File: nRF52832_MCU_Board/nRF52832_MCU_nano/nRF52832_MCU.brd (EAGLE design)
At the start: 55.7 x 22.9 mm, 56 parts, among them J1 TSW-116-02-S-S, J2 TSW-116-02-S-S, J3 MM8130-2600, J4 FPC_05P-RA-SMD, J5 DEBUG_CONNECTOR, U1 NRF52832, X1 32MHz, X2 32.768kHz, X3 TSW-102-02-S-S-RA, X4 TSW-102-02-S-S-RA, X5 TSW-103-02-S-S, X6 TSW-103-02-S-S

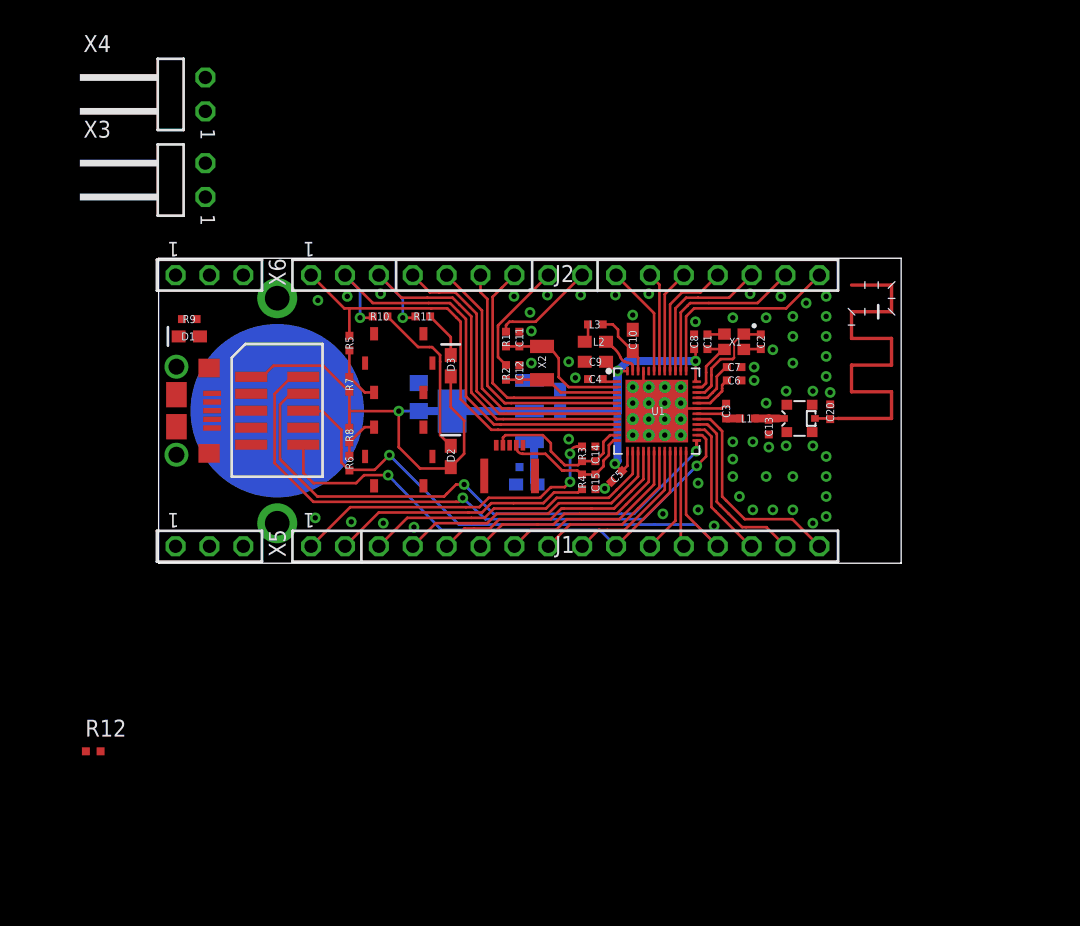
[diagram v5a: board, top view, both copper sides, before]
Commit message: Connected all signals in layout
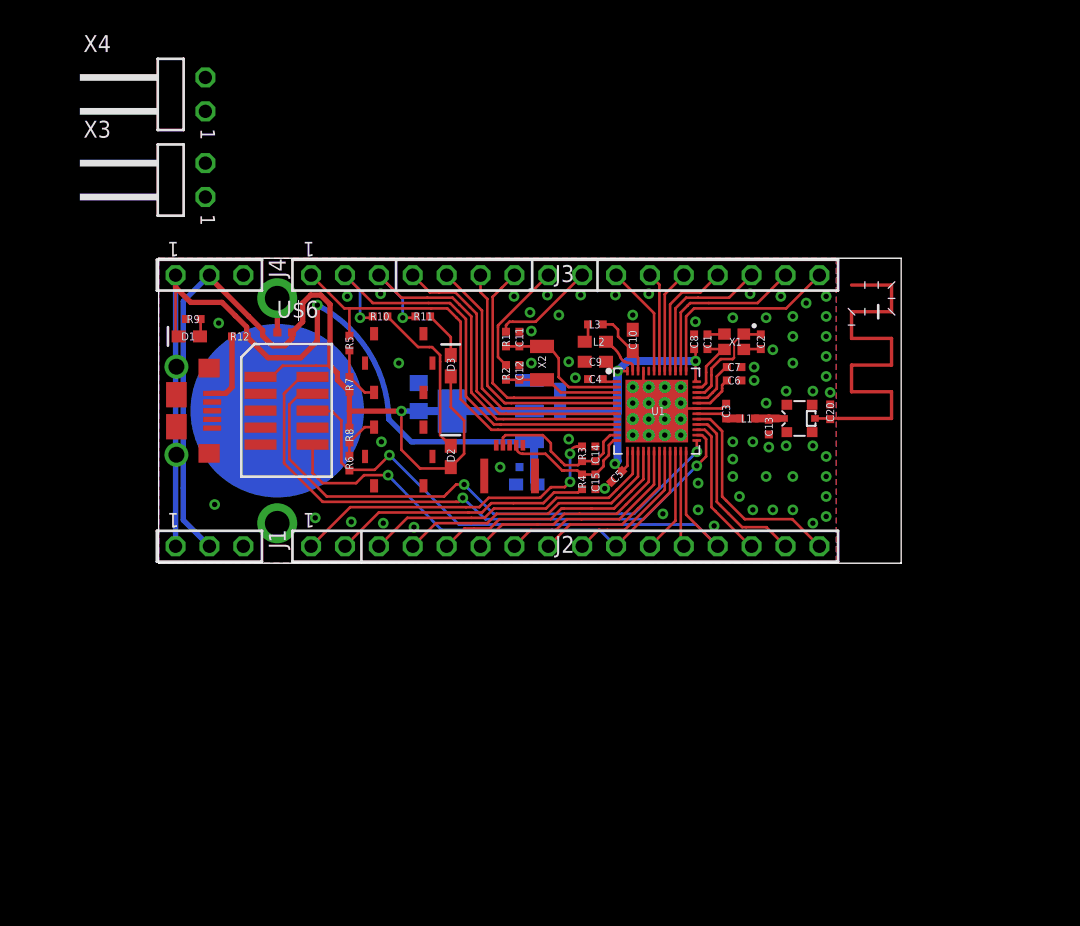
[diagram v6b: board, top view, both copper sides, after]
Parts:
- removed U$1: MICROUSB, Nordic_misc:USB-MICRO-B-RA-SMD-PIP
- removed X5, X6: TSW-103-02-S-S, con-samtec:TSW-103-02-S-S
- added J6: DEBUG_CONNECTOR, Nordic_misc:HDRV127P5X2-10_N
- added J7: FPC_05P-RA-SMD, Nordic_misc:FPC_05P-RA-SMD
- added J8: MM8130-2600, Nordic_misc:MM8130-2600
- added U$6: 0R, Nordic_misc:RESC0402_N
- C13: value (none) -> N.C.
- C20: value (none) -> TBD
- J1: value TSW-116-02-S-S -> TSW-103-02-S-S; device con-samtec:TSW-116-02-S-S -> con-samtec:TSW-103-02-S-S
- J3: value MM8130-2600 -> TSW-116-02-S-S; device Nordic_misc:MM8130-2600 -> con-samtec:TSW-116-02-S-S
- J4: value FPC_05P-RA-SMD -> TSW-103-02-S-S; device Nordic_misc:FPC_05P-RA-SMD -> con-samtec:TSW-103-02-S-S
- J5: value DEBUG_CONNECTOR -> MICROUSB; device Nordic_misc:HDRV127P5X2-10_N -> Nordic_misc:USB-MICRO-B-RA-SMD-PIP
- moved R12 33.0 mm to (6.05, 17.0)
- moved J4 26.7 mm to (3.81, 21.6), turned to 180 degrees
- moved J1 26.7 mm to (3.81, 1.27)
- moved J3 20.6 mm to (30.5, 21.6), turned to 180 degrees
- moved J2 20.3 mm to (30.5, 1.27)
- moved J5 4.88 mm to (4.01, 11.4), turned to 0 degrees
- moved R9 0.30 mm to (2.60, 18.3)
- renumbered U$2 to U2, U$3 to BATT1
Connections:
- new net VDD_P3V3_BATT: BATT1.2, BATT1.3, U$6.1
- net GND: now also BATT1.1, J1.3, J4.3, J6.3, J6.5, J6.9, J8.1, J8.2, J8.3, J8.4; no longer J3.1, J3.2, J3.3, J3.4, J5.3, J5.9, U$1.5, X5.3, X6.3
- net N$1: now also J8.OUT; no longer J3.OUT
- net N$5: now also J8.IN; no longer J3.IN
- net NFC1: now also J7.2; no longer J4.2
- net NFC2: now also J7.4; no longer J4.4
- net P0.00: now also J3.9; no longer J2.9
- net P0.01: now also J3.8; no longer J2.8
- net P0.02: now also J3.7; no longer J2.7
- net P0.03: now also J3.6; no longer J2.6
- net P0.04: now also J3.5; no longer J2.5
- net P0.05: now also J3.4; no longer J2.4
- net P0.06: now also J3.3; no longer J2.3
- net P0.07: now also J3.2; no longer J2.2
- net P0.08: now also J3.1; no longer J2.1
- net P0.09: now also J2.1; no longer J1.1
- net P0.10: now also J2.2; no longer J1.2
- net P0.11: now also J2.3; no longer J1.3
- net P0.12: now also J2.4; no longer J1.4
- net P0.13: now also J2.5; no longer J1.5
- net P0.14: now also J2.6; no longer J1.6
- net P0.15: now also J2.7; no longer J1.7
- net P0.16: now also J2.8; no longer J1.8
- net P0.17: now also J2.9; no longer J1.9
- net P0.18/SWO: now also J2.10, J6.10; no longer J1.10, J5.10
- net P0.19: now also J2.11; no longer J1.11
- net P0.20: now also J2.12; no longer J1.12
- net P0.21/RESET: now also J2.13, J6.6; no longer J1.13, J5.6
- net P0.22: now also J2.14; no longer J1.14
- net P0.23: now also J2.15; no longer J1.15
- net P0.24: now also J2.16; no longer J1.16
- net P0.25: now also J3.16; no longer J2.16
- net P0.26: now also J3.15; no longer J2.15
- net P0.27: now also J3.14; no longer J2.14
- net P0.28: now also J3.13; no longer J2.13
- net P0.29: now also J3.12; no longer J2.12
- net P0.30: now also J3.11; no longer J2.11
- net P0.31: now also J3.10; no longer J2.10
- net SWDCLK: now also J6.4; no longer J5.4
- net SWDIO: now also J6.2; no longer J5.2
- net VCC_P5V0_USB: now also J5.1; no longer U$1.1
- net VDD_P3V3: now also J1.2, J4.2, J6.1, U$6.2; no longer J5.1, X5.2, X6.2
- net VDD_P5V0: now also J1.1, J4.1; no longer X5.1, X6.1
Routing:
- net VDD_P5V0: track 3.45 -> 67.1 mm, vias 0 -> 1
- net VDD_P3V3: track 70.9 -> 111.4 mm
- net VCC_P5V0_USB: track 0.00 -> 5.48 mm
- net VDD_P3V3_BATT: track 0.00 -> 2.57 mm
- net SWDCLK: track 43.4 -> 41.9 mm
- net VDD_LED: track 0.00 -> 1.30 mm
- net SWDIO: track 46.2 -> 45.5 mm
- net P0.18/SWO: track 37.2 -> 36.5 mm
- net GND: vias 63 -> 67
- added copper zone on layer 1, net GND
- added copper zone on layer 16, net GND

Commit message: Looked at arduino layout
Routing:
- net N$7: track 4.33 -> 6.69 mm
- net GND: vias 67 -> 68
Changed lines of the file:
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@@
 <grid distance="0.1" unitdist="mm" unit="mm" style="lines" multiple="2" display="yes" altdistance="0.05" altunitdist="mm" altunit="mm"/>
 <layers>
-<layer number="1" name="Top" color="4" fill="1" visible="no" active="yes"/>
+<layer number="1" name="Top" color="4" fill="1" visible="yes" active="yes"/>
 <layer number="16" name="Bottom" color="1" fill="1" visible="yes" active="yes"/>
 <layer number="17" name="Pads" color="2" fill="1" visible="yes" active="yes"/>
@@
 <via x="4.2" y="4.4" extent="1-16" drill="0.4"/>
 <via x="4.5" y="18" extent="1-16" drill="0.4"/>
-<wire x1="19.85" y1="17.2" x2="20.525" y2="15" width="0" layer="19" extent="1-1"/>
+<via x="20.9" y="16.9" extent="1-16" drill="0.4"/>
 </signal>
 <signal name="DEC1">
@@
 <wire x1="14.3" y1="13.95" x2="15.45" y2="12.8" width="0.2" layer="1"/>
 <wire x1="15.45" y1="12.8" x2="16.15" y2="12.8" width="0.2" layer="1"/>
-<wire x1="14.3" y1="15.95" x2="16.15" y2="17.2" width="0" layer="19" extent="1-1"/>
+<wire x1="14.3" y1="15.95" x2="15.55" y2="17.2" width="0.2" layer="1"/>
+<wire x1="15.55" y1="17.2" x2="16.15" y2="17.2" width="0.2" layer="1"/>
 </signal>
 <signal name="VDD_P3V3">

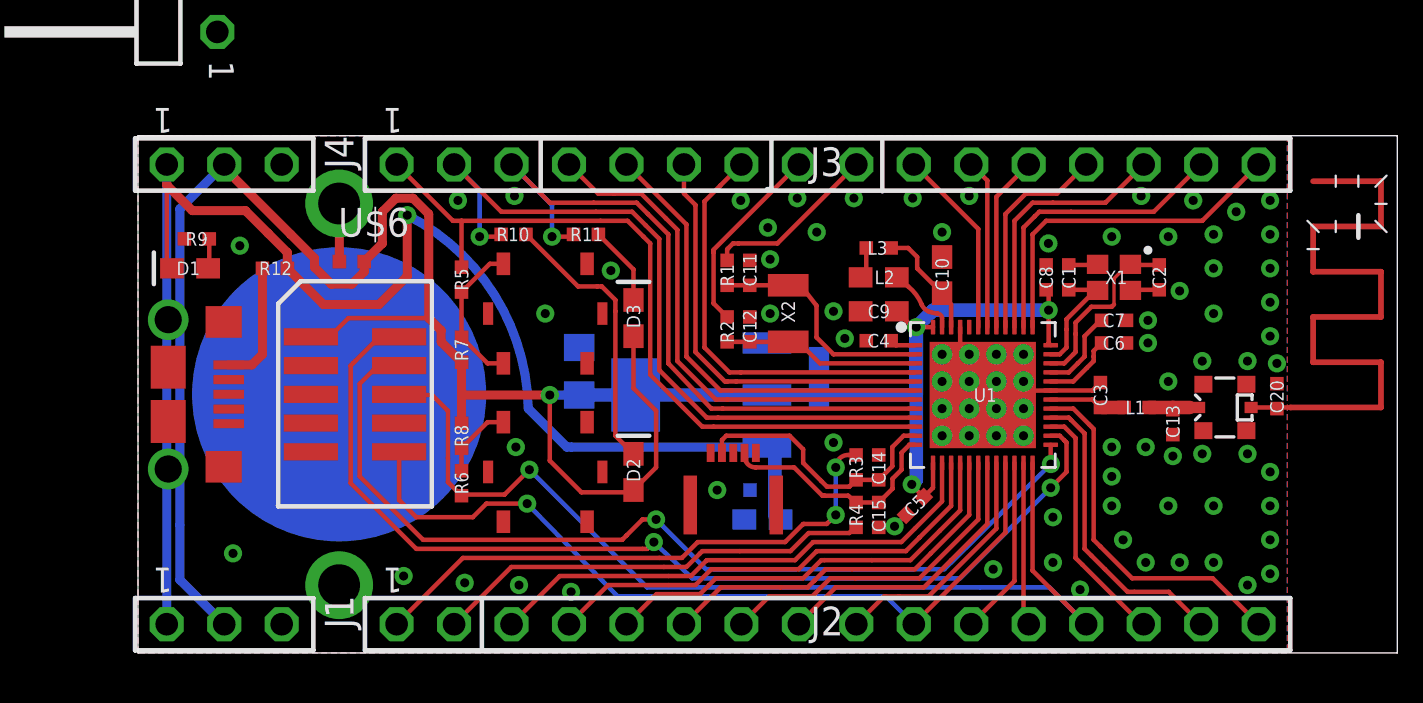
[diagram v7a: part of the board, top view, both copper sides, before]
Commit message: Cleanup in layout
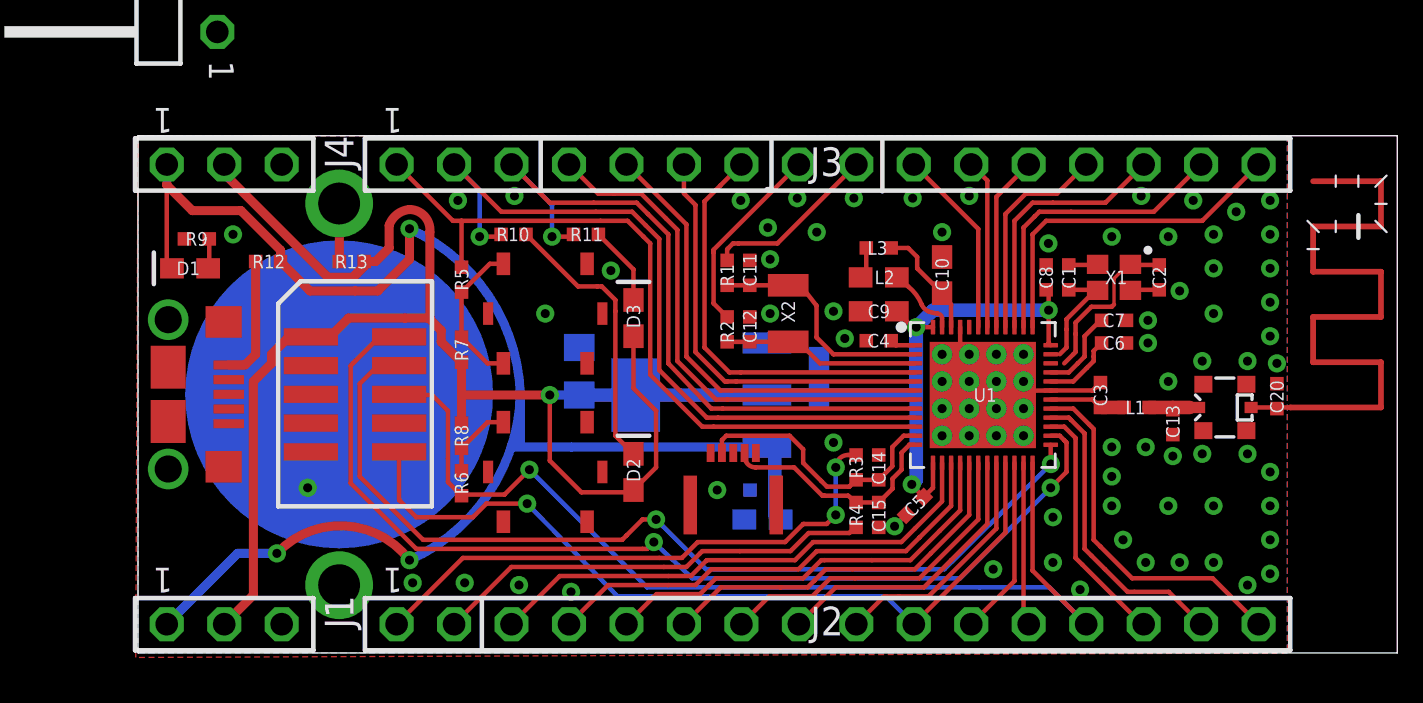
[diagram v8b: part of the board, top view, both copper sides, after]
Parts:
- moved R12 0.42 mm to (5.75, 17.3)
- renumbered U$6 to R13
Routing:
- net GND: track 28.3 -> 65.7 mm, vias 68 -> 67
- net VDD_P3V3: track 111.4 -> 104.0 mm
- net VDD_P5V0: track 67.1 -> 68.1 mm, vias 1 -> 3
- net X1: track 8.06 -> 7.46 mm
